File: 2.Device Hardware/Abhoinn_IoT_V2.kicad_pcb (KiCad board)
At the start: 4 copper layers, 96 x 96 mm, 46 parts, among them IC1 AX-SIP-SFEU-1-01-TX30, IC2 MS5840-02BA01, J1 Conn_01x02, J2 Conn_01x02, J3 Conn_02x05_Odd_Even, J4 Conn_02x05_Odd_Even, J5 Conn_Coaxial, J6 Conn_01x02_Female, P1 USB_C_Plug_USB2.0, U1 XC6206PxxxMR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

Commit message: update
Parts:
- moved J5 1.38 mm to (121.6, 79.3)
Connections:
- F1 pad 2: Net-(D1-Pad1) -> Net-(F1-Pad2)
- FB1 pad 1: Net-(D1-Pad1) -> Net-(F1-Pad2)
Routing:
- net GND: track 30.7 -> 65.8 mm, vias 16 -> 63
- net Net-(P1-PadS1): track 0.00 -> 30.1 mm
- net Net-(D4-Pad2): track 8.10 -> 34.5 mm
- net +5V: track 54.5 -> 70.1 mm
- net Net-(P1-PadA4): track 0.00 -> 5.96 mm
- net Net-(F1-Pad2): track 0.00 -> 5.06 mm
- net Net-(D1-Pad1): track 10.1 -> 5.08 mm
- net +3V3: track 44.8 -> 42.0 mm, vias 9 -> 23
- net Net-(IC1-Pad3): track 10.1 -> 8.60 mm
- net (no net): vias 0 -> 1
- added copper zone on In2.Cu, net +3V3
- added copper zone on In1.Cu, net GND

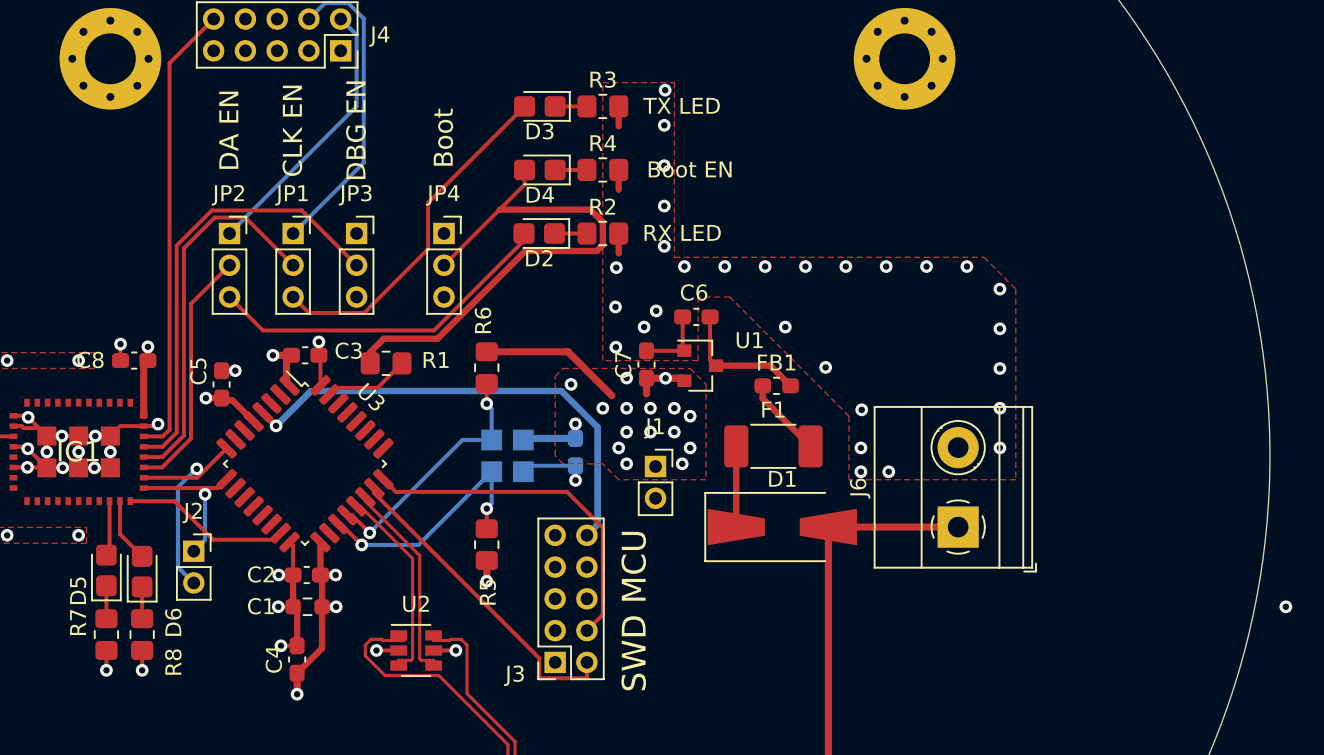
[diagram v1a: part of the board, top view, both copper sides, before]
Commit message: Updatre fuese
Supply issure, footprint swap for 500mA fuse
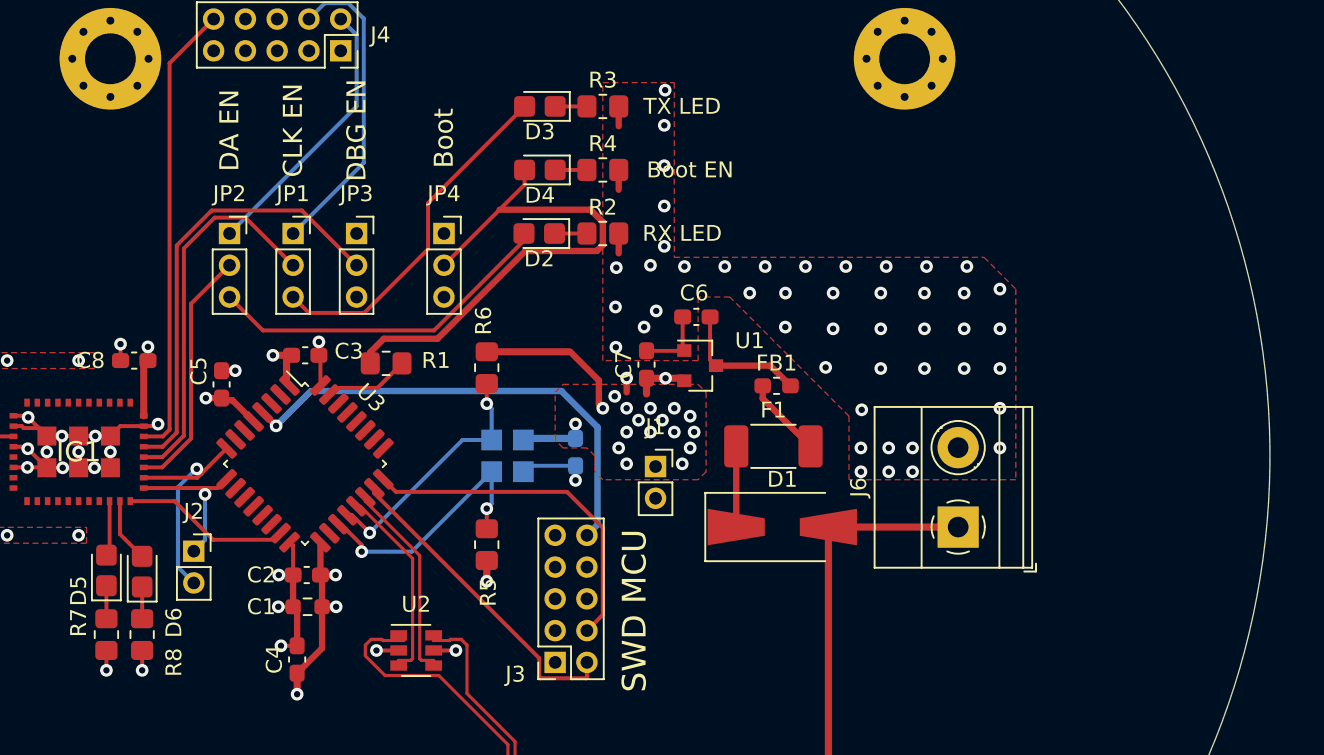
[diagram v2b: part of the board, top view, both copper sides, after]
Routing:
- net +3V3: track 42.0 -> 43.5 mm, vias 23 -> 26
- net PRESSURE_SCL: track 15.8 -> 16.5 mm
- net GND: vias 63 -> 80
- net (no net): vias 1 -> 0

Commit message: minor update
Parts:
- F1: footprint Fuse:Fuse_2010_5025Metric_Pad1.52x2.65mm_HandSolder -> Fuse:Fuse_1210_3225Metric_Pad1.42x2.65mm_HandSolder
